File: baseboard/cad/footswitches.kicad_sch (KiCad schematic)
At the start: 21 parts, among them J12 6-440054-2, J13 6-440054-2, J14 6-440129-2, J15 6-440129-2, J17 6-440054-2, J18 6-440054-2, J19 6-440129-2, J20 6-440129-2, Q1 Q_Dual_NMOS_S1G1D2S2G2D1, SW1 FOOTSWITCH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

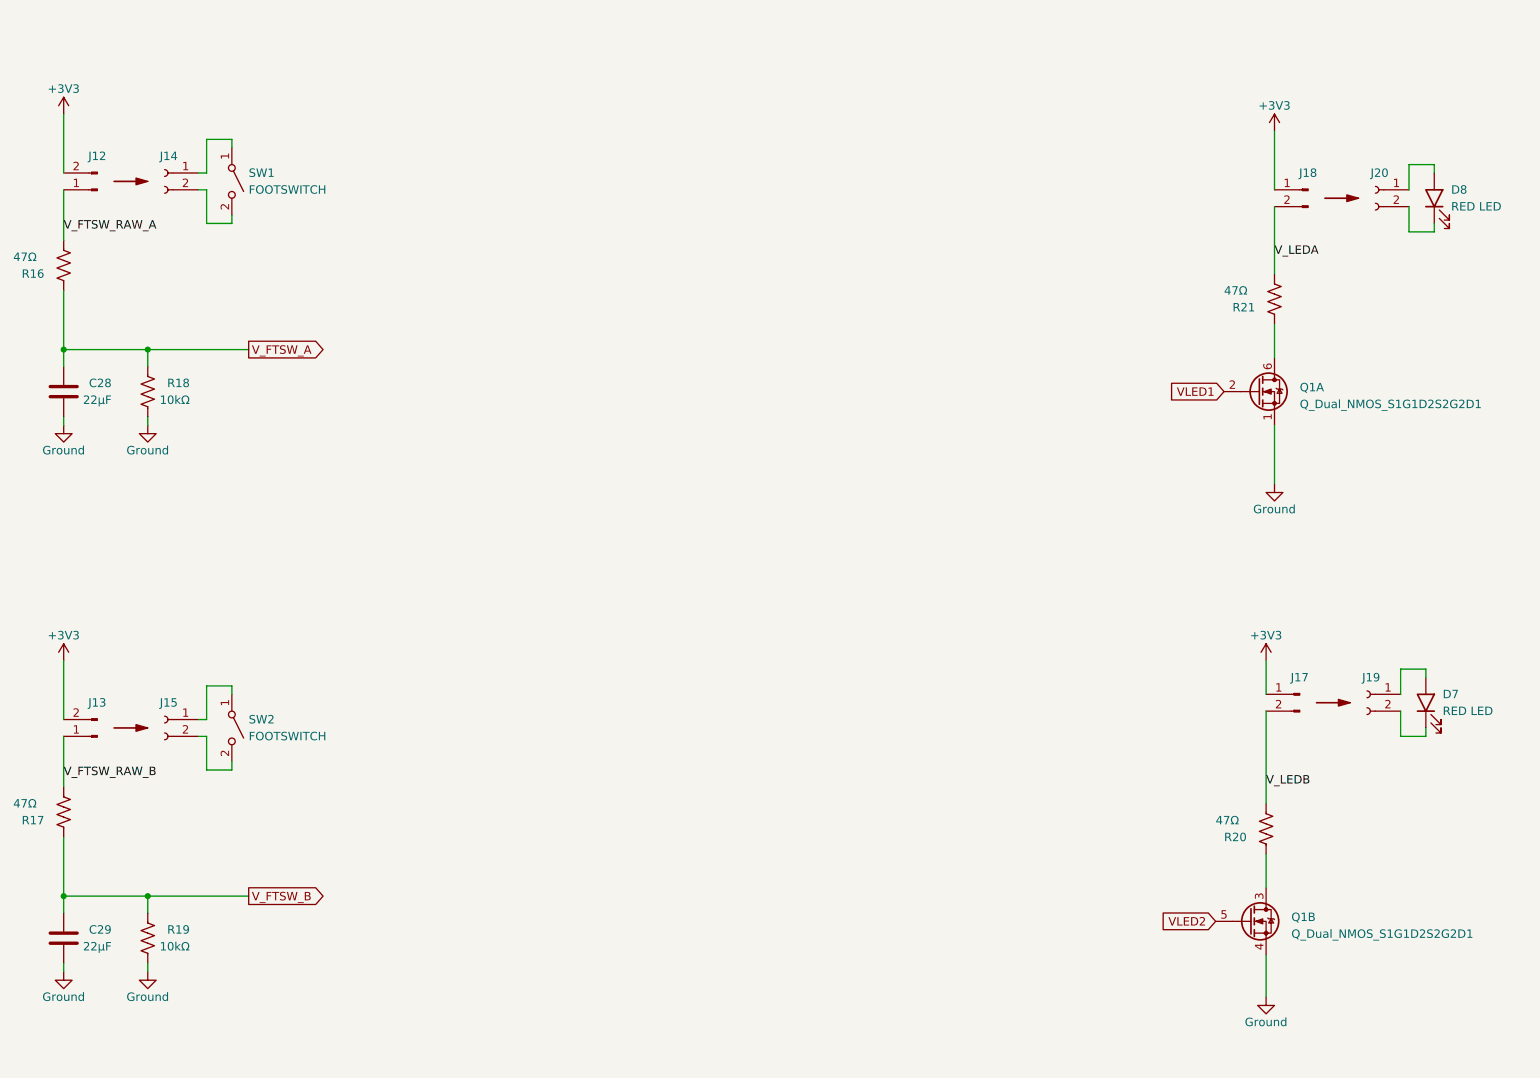
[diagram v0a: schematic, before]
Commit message: added microcontroller enable to analog power rails
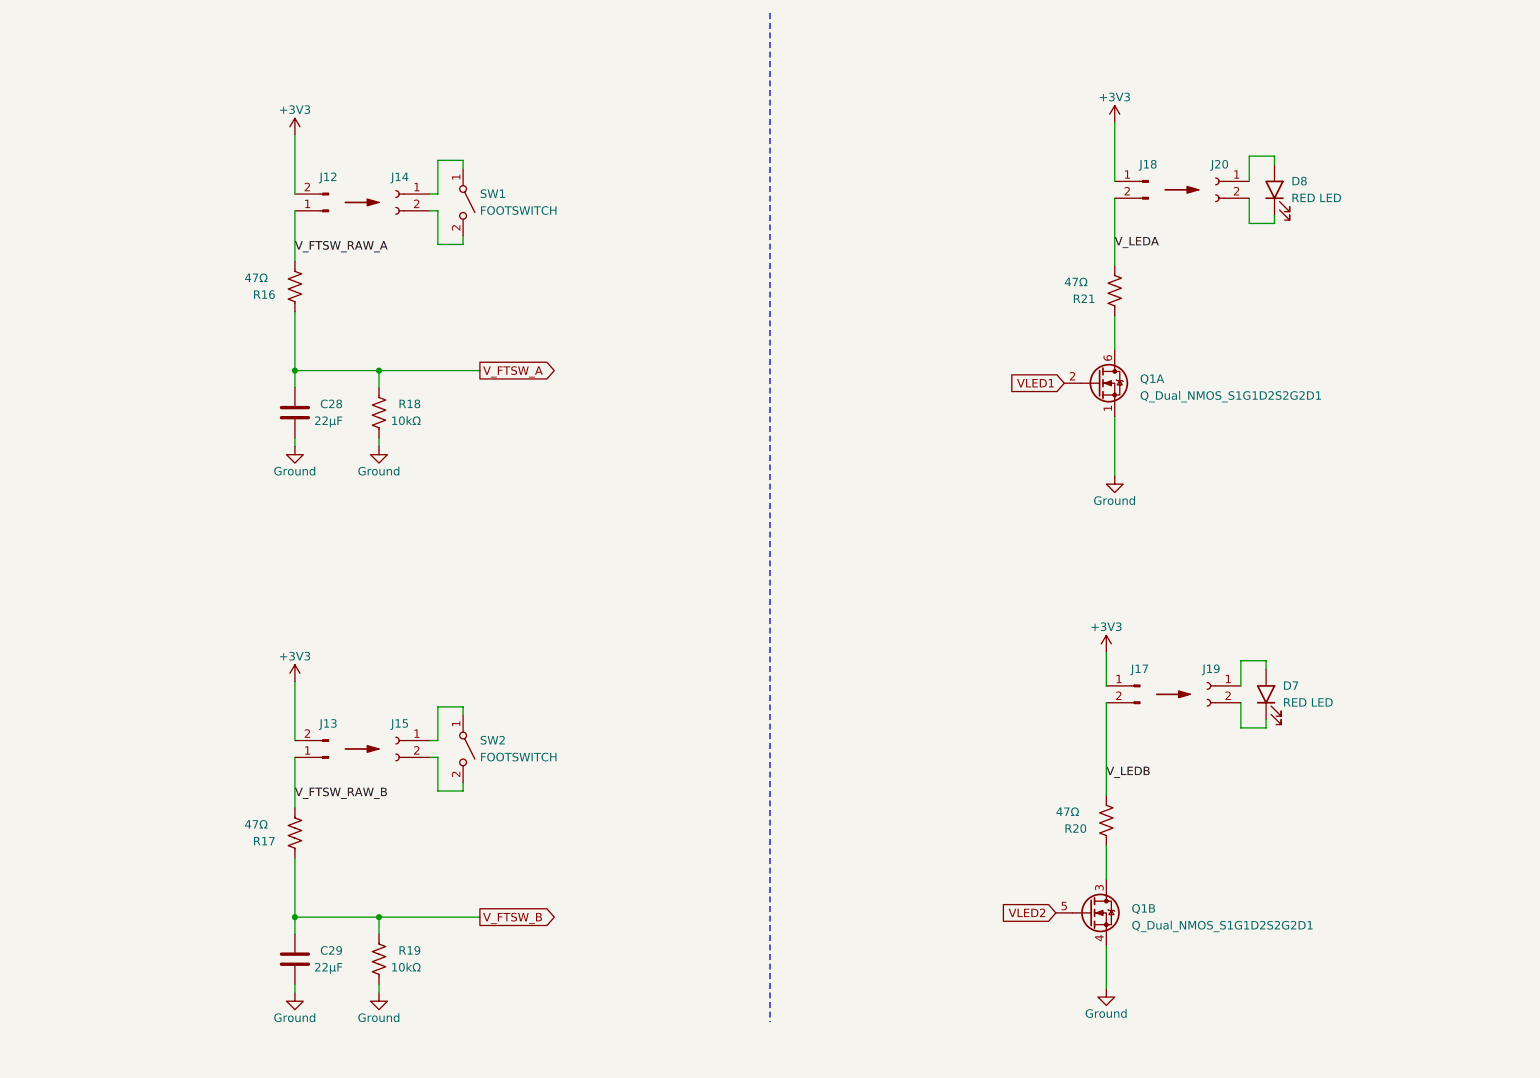
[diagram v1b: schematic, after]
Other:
- moved on the sheet: C28, C29, D7, D8, J12, J13, J14, J15, J17, J18, J19, J20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

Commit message: added reset button to microcontroller
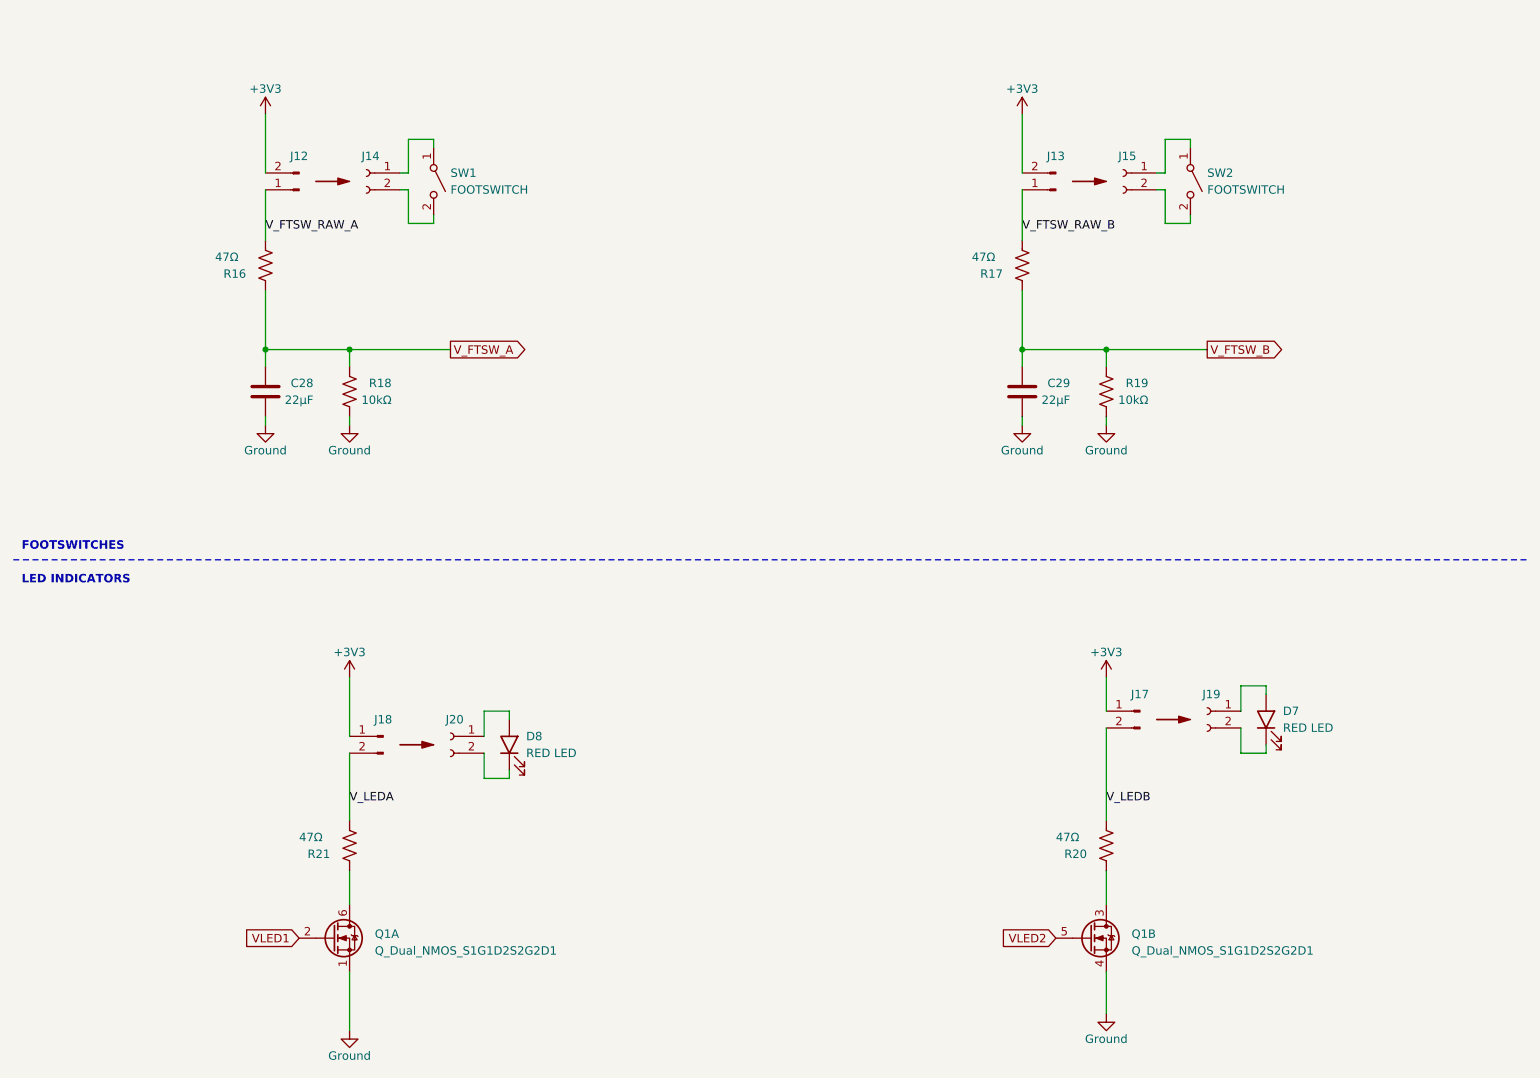
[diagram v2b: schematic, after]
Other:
- note added: "FOOTSWITCHES"
- note added: "LED INDICATORS"
- moved on the sheet: C28, C29, D7, D8, J12, J13, J14, J15, J17, J18, J19, J20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

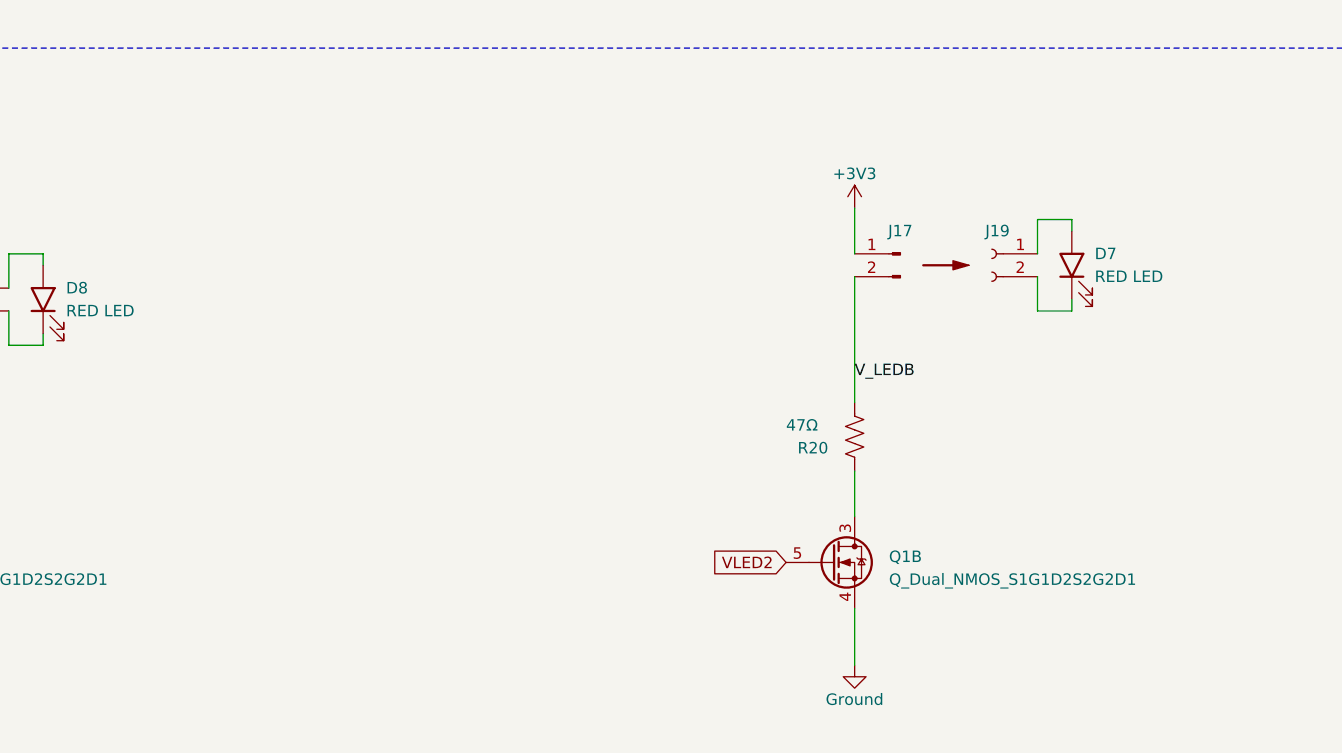
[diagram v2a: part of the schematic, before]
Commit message: placed components and finished new micro hw
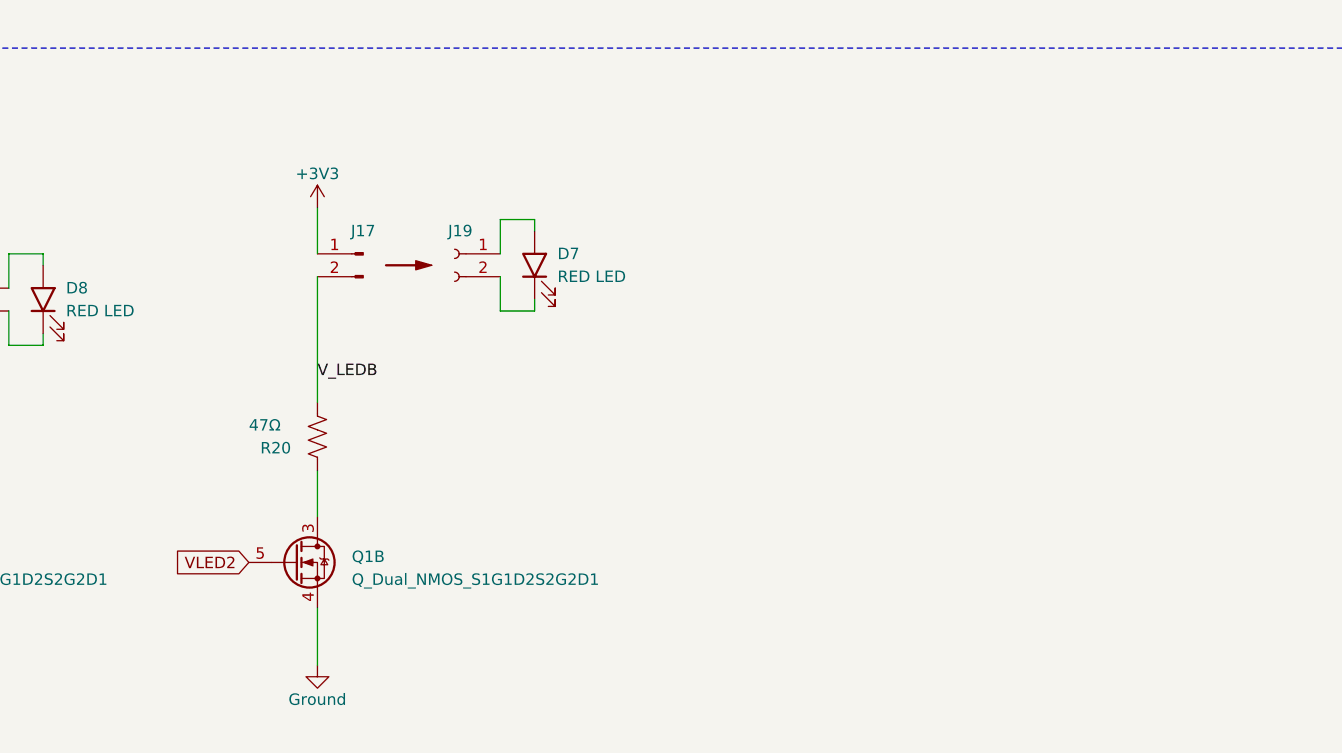
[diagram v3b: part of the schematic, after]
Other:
- moved on the sheet: D7, J17, J19, Q1B, R20
